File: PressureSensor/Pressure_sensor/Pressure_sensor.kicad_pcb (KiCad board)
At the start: 2 copper layers, 79 x 96.3 mm, 78 parts, among them J1 Power Input, J2 Conn_01x04_Pin, J3 Screw_Terminal_01x03, J4 Conn_02x03_Odd_Even, J5 Valve Terminal, J6 Conn_01x05_Pin, J7 USB_A, K1 SANYOU_SRD_Form_C, Q1 BC848, SW1 SW_SPST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

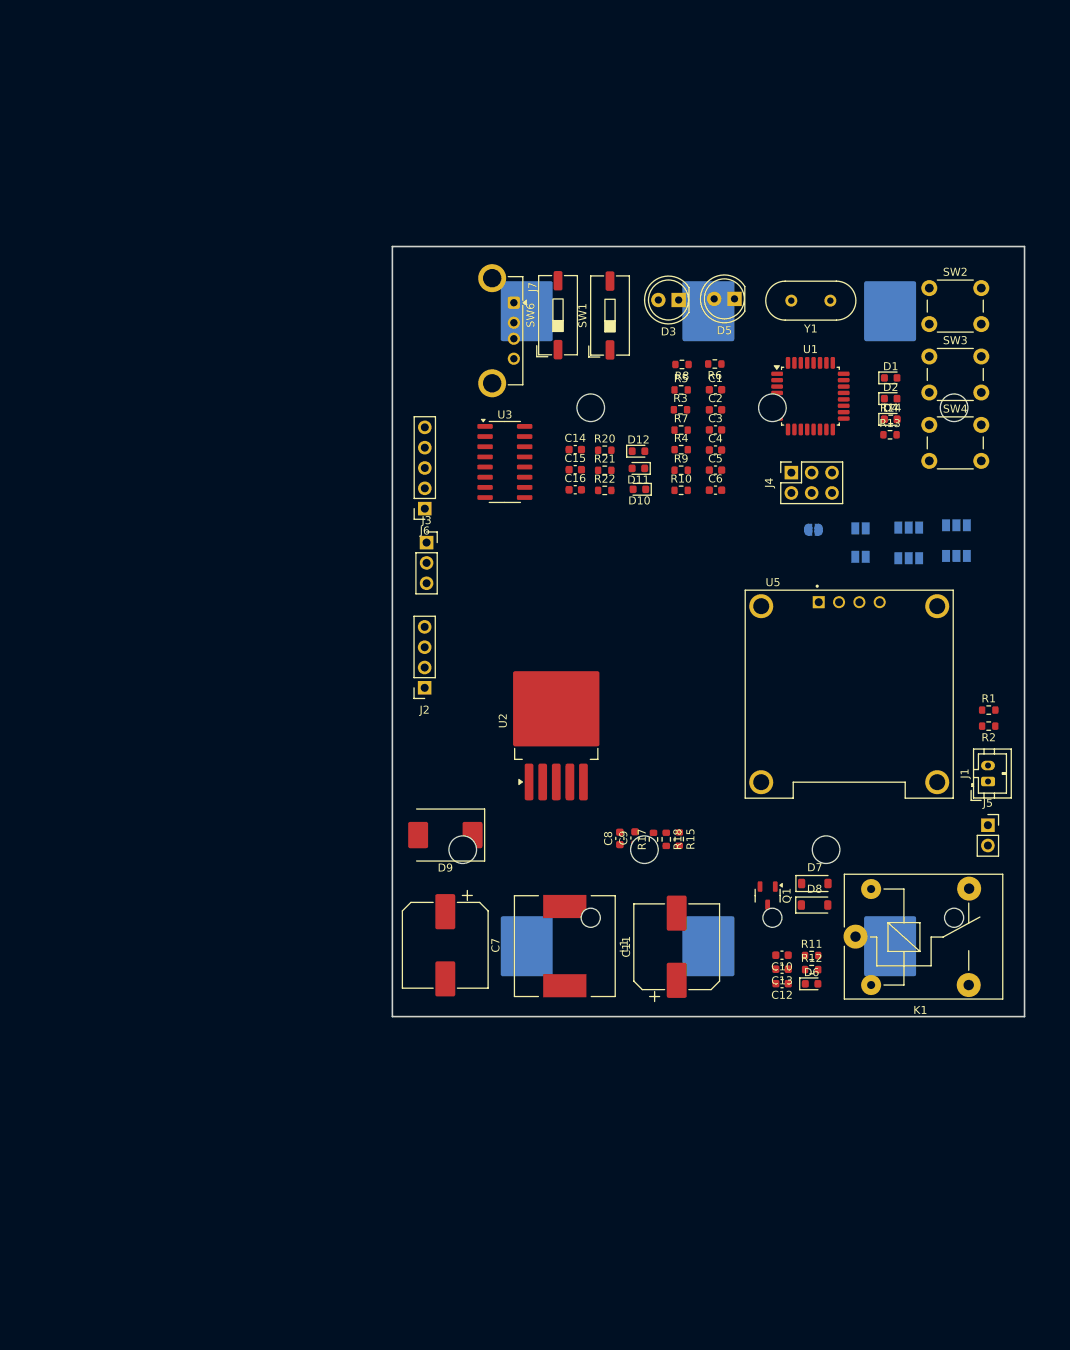
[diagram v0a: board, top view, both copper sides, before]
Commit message: For Checking
- Data tracks
- Components placement

do not mind the ff will do after this checking:
- power tracks - zoning
- zone layer
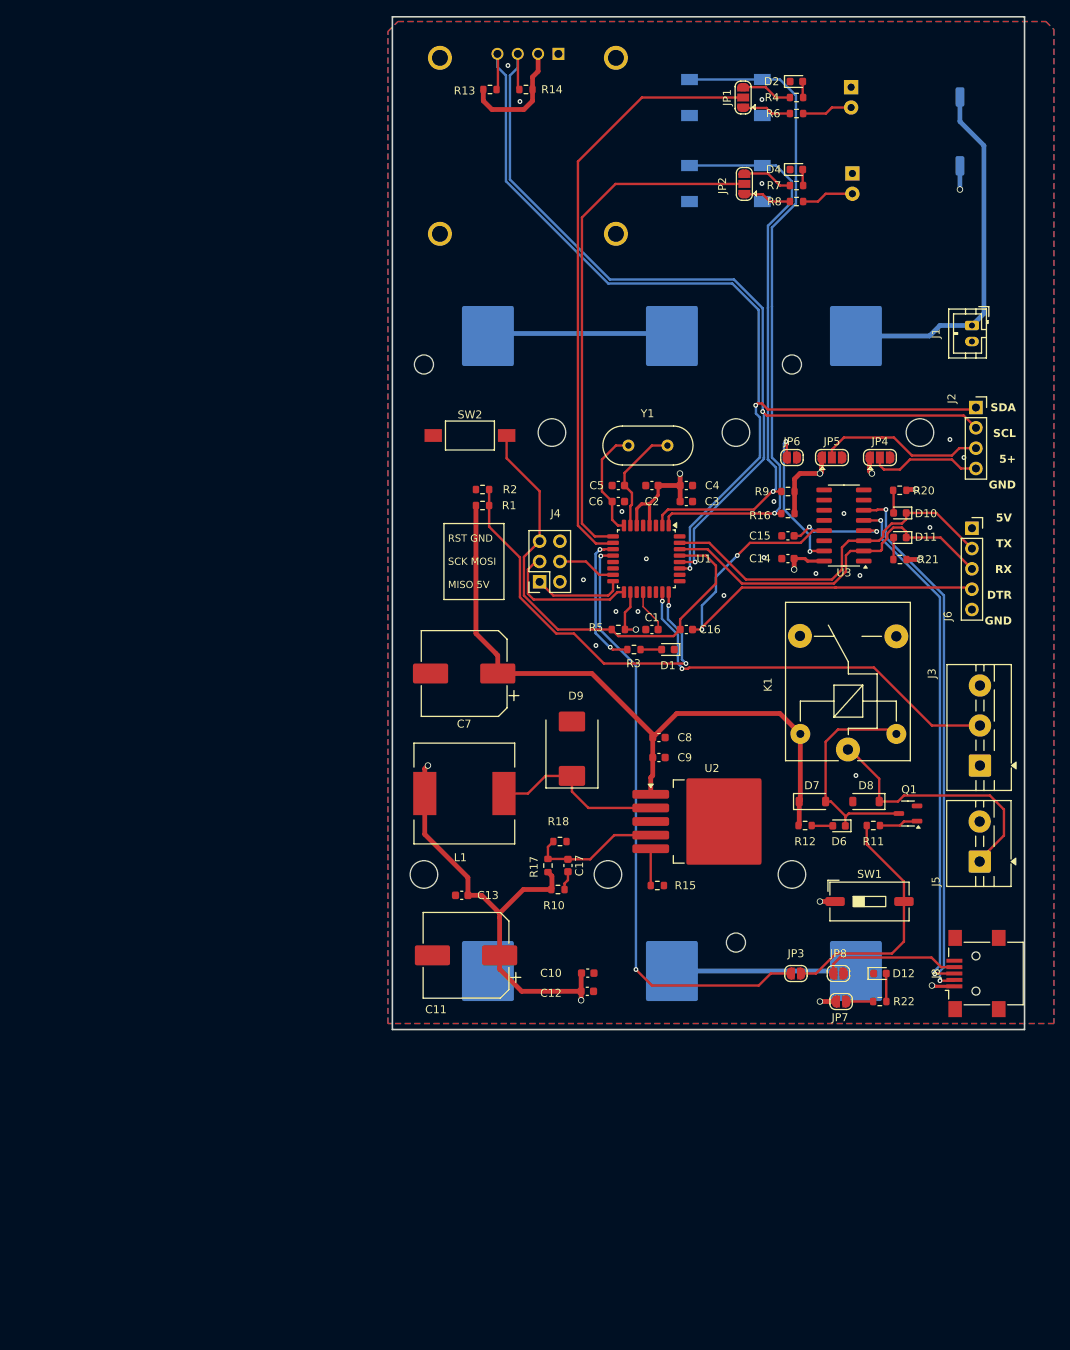
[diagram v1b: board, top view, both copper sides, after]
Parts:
- removed J7: USB_A, Connector_USB:USB_A_Connfly_DS1095
- removed SW3, SW4: SW_Push, Button_Switch_THT:SW_PUSH_6mm_H9.5mm
- added C17: 3300pF, Capacitor_SMD:C_0603_1608Metric, F.Cu at (155.0, 103.5)
- added J8: USB_B_Mini, Connector_USB:USB_Mini-B_Lumberg_2486_01_Horizontal, F.Cu at (206.0, 117.0)
- added JP8: SolderJumper_2_Open, Jumper:SolderJumper-2_P1.3mm_Open_RoundedPad1.0x1.5mm, F.Cu at (188.8, 117.0)
- added R16: 1K, Resistor_SMD:R_0603_1608Metric, F.Cu at (182.5, 59.5)
- added S3: TS04-66-70-BK-160-SMT, TS04-66-70-BK-160-SMT:SW_TS04-66-70-BK-160-SMT, B.Cu at (174.8, 18.2)
- added S4: TS04-66-70-BK-160-SMT, TS04-66-70-BK-160-SMT:SW_TS04-66-70-BK-160-SMT, B.Cu at (174.8, 7.50)
- D3, D5, SW6, U5: moved to B.Cu
- J3: footprint Connector_PinSocket_2.54mm:PinSocket_1x03_P2.54mm_Vertical -> TerminalBlock:TerminalBlock_MaiXu_MX126-5.0-03P_1x03_P5.00mm
- J5: footprint Connector_PinSocket_2.54mm:PinSocket_1x02_P2.54mm_Vertical -> TerminalBlock:TerminalBlock_MaiXu_MX126-5.0-02P_1x02_P5.00mm
- JP1, JP2, JP4, JP5: footprint Jumper:SolderJumper-3_P1.3mm_Open_Pad1.0x1.5mm -> Jumper:SolderJumper-3_P1.3mm_Open_RoundedPad1.0x1.5mm; moved to F.Cu
- JP3: moved to F.Cu
- JP6, JP7: footprint Jumper:SolderJumper-2_P1.3mm_Open_Pad1.0x1.5mm -> Jumper:SolderJumper-2_P1.3mm_Open_RoundedPad1.0x1.5mm; moved to F.Cu
- R10: value 1K -> 100
- SW2: footprint Button_Switch_THT:SW_PUSH_6mm_H9.5mm -> Button_Switch_SMD:SW_SPST_FSMSM
- moved SW1 80.1 mm to (192.7, 108.0), turned to 0 degrees
- moved U5 79.4 mm to (150.0, 13.5), turned to 180 degrees
- moved J2 77.3 mm to (206.0, 46.2), turned to 0 degrees
- moved J3 74.6 mm to (206.5, 91.0), turned to 90 degrees
- moved R22 72.6 mm to (194.0, 120.5)
- moved D12 71.9 mm to (194.0, 117.0)
- moved R2 69.8 mm to (144.3, 56.5), turned to 0 degrees
- moved J6 68.4 mm to (205.5, 61.3), turned to 0 degrees
- moved R1 68.2 mm to (144.3, 58.5), turned to 180 degrees
- moved R13 66.1 mm to (145.2, 6.50), turned to 180 degrees
- moved R14 61.5 mm to (149.8, 6.50)
- moved SW2 60.3 mm to (142.8, 49.8)
- moved JP1 59.7 mm to (176.9, 7.50), turned to 90 degrees
- moved J1 57.0 mm to (205.5, 36.0), turned to -90 degrees
- moved JP7 55.6 mm to (189.2, 120.5)
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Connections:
- BT1 pad 1: +12V -> Net-(BT1-+)
- BT2 pad 1: GND -> Net-(BT2-+)
- BT2 pad 2: +12V -> Net-(BT1-+)
- BT3 pad 1: +12V -> +BATT
- BT3 pad 2: GND -> Net-(BT2-+)
- C14 pad 1: VBUS -> +5V
- J1 pad 1: Net-(J1-Pin_1) -> +BATT
- JP7 pad 2: VBUS -> +5V
- R10 pad 1: +5V -> Net-(C17-Pad2)
- R10 pad 2: Net-(U1-PD3) -> +5V
- R20 pad 1: VBUS -> +5V
- R21 pad 1: VBUS -> +5V
- SW1 pad 1: GND -> +5V
- SW6 pad 1: Net-(J1-Pin_1) -> +BATT
- U3 pad 16: VBUS -> +5V
- U5 pad S1: (no net) -> GND
- U5 pad S2: (no net) -> GND
- U5 pad S3: (no net) -> GND
- U5 pad S4: (no net) -> GND
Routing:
- net +5V: track 0.00 -> 473.4 mm, vias 0 -> 12
- net +12V: track 0.00 -> 175.5 mm, vias 0 -> 1
- net SDA: track 0.00 -> 124.8 mm, vias 0 -> 2
- net SCL: track 0.00 -> 123.9 mm, vias 0 -> 2
- net Net-(U1-PD3): track 0.00 -> 83.6 mm, vias 0 -> 1
- net RLY_CTRL: track 0.00 -> 75.9 mm, vias 0 -> 2
- net Net-(JP1-C): track 0.00 -> 74.8 mm
- net Net-(U1-PD4): track 0.00 -> 71.6 mm, vias 0 -> 1
- net D-: track 0.00 -> 66.8 mm, vias 0 -> 2
- net Net-(JP2-C): track 0.00 -> 64.9 mm
- net D+: track 0.00 -> 64.6 mm, vias 0 -> 2
- net DTR: track 0.00 -> 60.6 mm, vias 0 -> 2
- net ARDU_RST: track 0.00 -> 59.4 mm
- net PSensor: track 0.00 -> 50.9 mm, vias 0 -> 2
- net Vsense: track 0.00 -> 49.1 mm, vias 0 -> 2
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- added copper zone on B.Cu, net GND
- added copper zone on F.Cu, net GND
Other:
- board size 79 x 96.3 mm -> 79 x 126.6 mm
- copper layers 2 -> 4
- board text added: "5V TX RX DTR GND"
- board text added: "RST GND SCK MOSI MISO 5V"
- board text added: "SDA SCL 5+ GND"

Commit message: Habol lang
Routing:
- added copper zone on In1.Cu, net GND
- added copper zone on In2.Cu, net GND
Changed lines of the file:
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@@
 		(net 2)
 		(net_name "GND")
-		(layers "F.Cu" "B.Cu")
+		(layers "F.Cu" "B.Cu" "In1.Cu" "In2.Cu")
 		(hatch edge 0.5)
 		(connect_pads

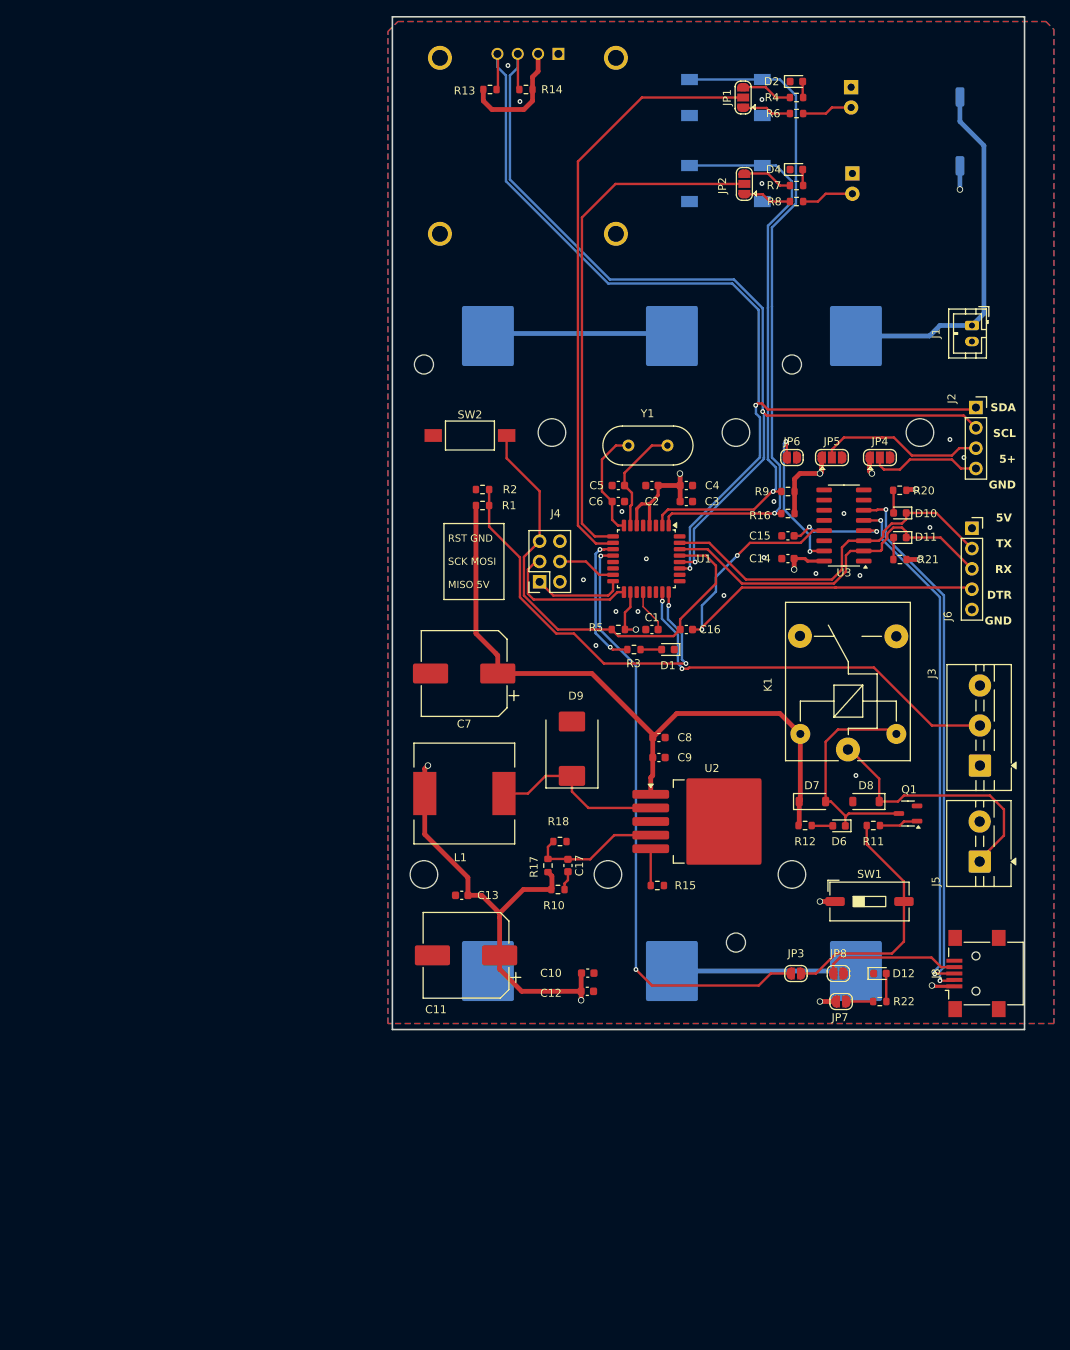
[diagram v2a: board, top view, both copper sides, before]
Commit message: initial checking for final placement
For checking
1. tracks std
2. zones
3. layering
4, placement
5. ERC std
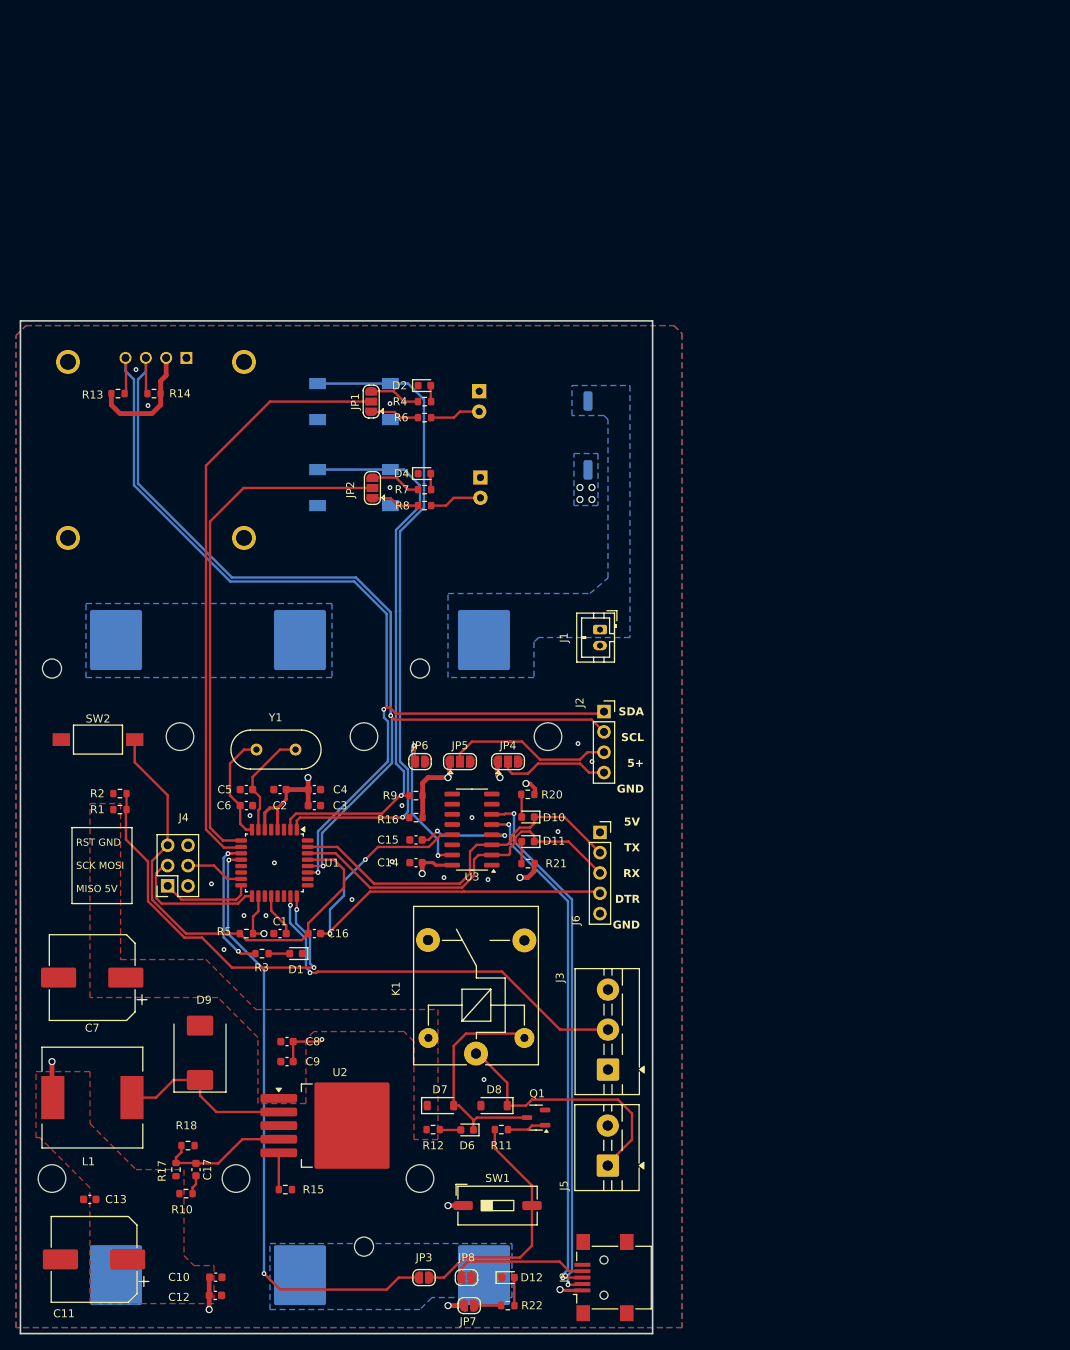
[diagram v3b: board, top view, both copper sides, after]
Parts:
- moved R11 60.1 mm to (146.7, 136.5)
- moved D6 60.1 mm to (142.4, 136.5)
- moved C12 60.1 mm to (110.9, 157.2)
- moved C16 60.1 mm to (123.3, 112.0)
- moved C3 60.1 mm to (123.3, 96.0)
- moved C4 60.1 mm to (123.3, 94.0)
- moved C5 60.1 mm to (114.8, 94.0)
- moved C6 60.1 mm to (114.8, 96.0)
- moved C7 60.1 mm to (95.5, 117.5)
- moved J4 60.1 mm to (105.0, 106.0)
- moved L1 60.1 mm to (95.6, 132.5)
- moved R15 60.1 mm to (119.7, 144.0)
- moved R5 60.1 mm to (114.8, 112.0)
- moved U1 60.1 mm to (118.3, 103.2)
- moved C11 60.1 mm to (95.8, 152.7)
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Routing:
- net +5V: track 473.4 -> 88.4 mm
- net +12V: track 175.5 -> 0.00 mm, vias 1 -> 4
- net +BATT: track 45.5 -> 0.00 mm
- net Net-(BT1-+): track 23.3 -> 0.00 mm
- net Net-(BT2-+): track 23.0 -> 0.00 mm
- net GND: track 0.00 -> 6.20 mm, vias 20 -> 21
- added copper zone on B.Cu, net +12V
- added copper zone on F.Cu, net +12V
- added copper zone on In2.Cu, net +12V
- added copper zone on F.Cu, net +5V
- added copper zone on In2.Cu, net +5V
- added copper zone on B.Cu, net +BATT
- added copper zone on B.Cu, net Net-(BT1-+)
- added copper zone on B.Cu, net Net-(BT2-+)
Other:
- board text added: "ON"

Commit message: Reviewed by Nes
DONE
1. each GND pad have via
2. heatsink for U2 and ATMEGA

for clarification
1. added mounting holes
2. added silk for jumper wires?
3. Where to put LCSC number
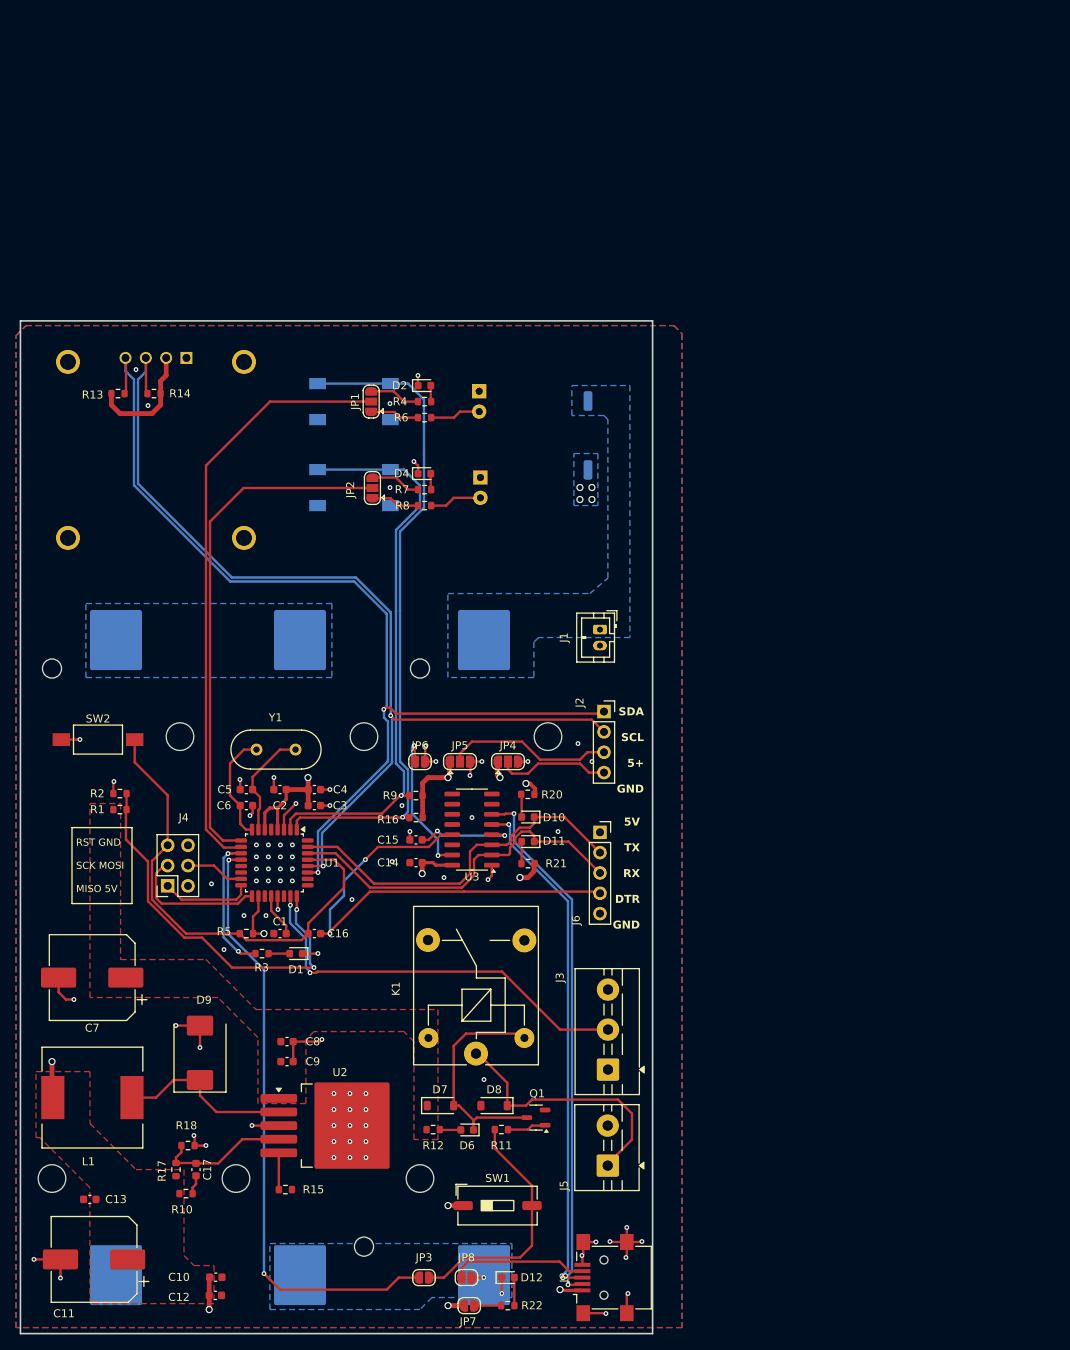
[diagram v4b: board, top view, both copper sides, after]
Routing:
- net GND: track 6.20 -> 80.9 mm, vias 21 -> 86
